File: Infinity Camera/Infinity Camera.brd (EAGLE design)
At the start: 115.6 x 54.6 mm, 7 parts

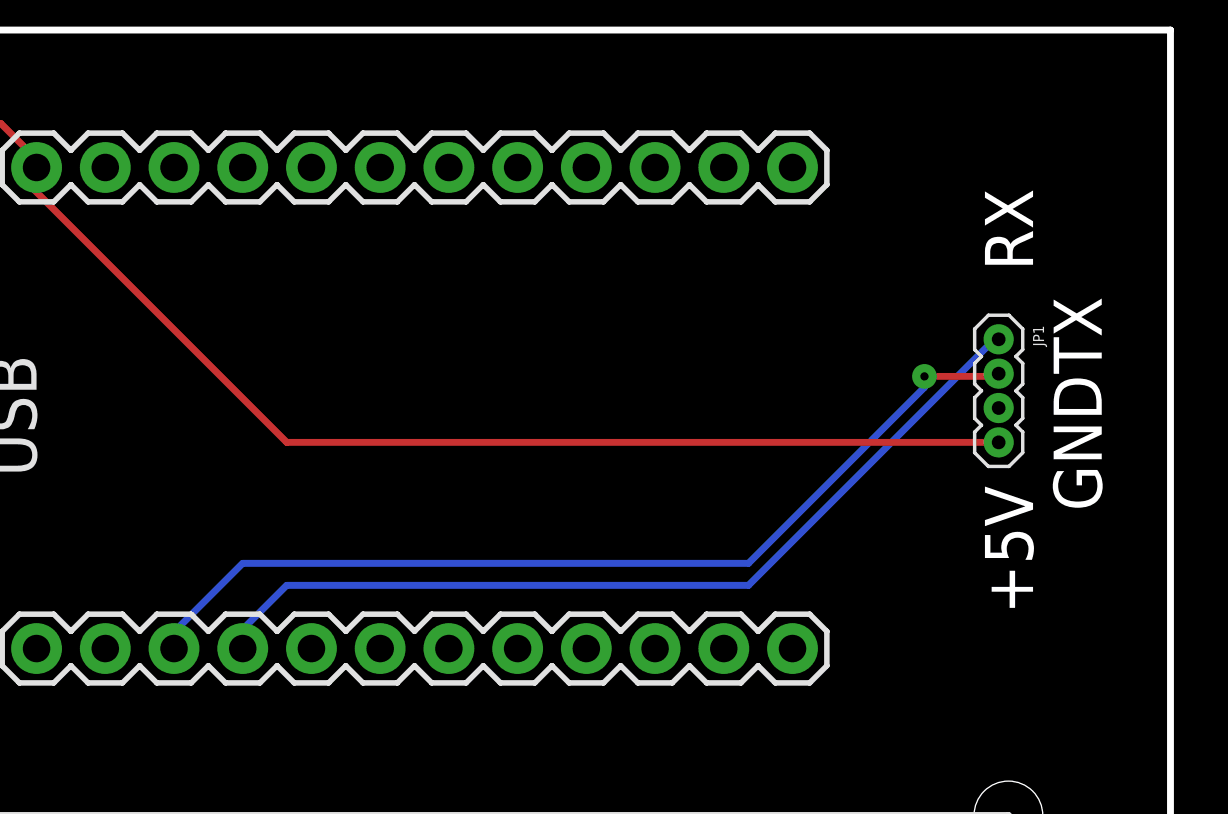
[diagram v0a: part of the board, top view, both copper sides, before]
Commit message: Reviewed Infinity Camera
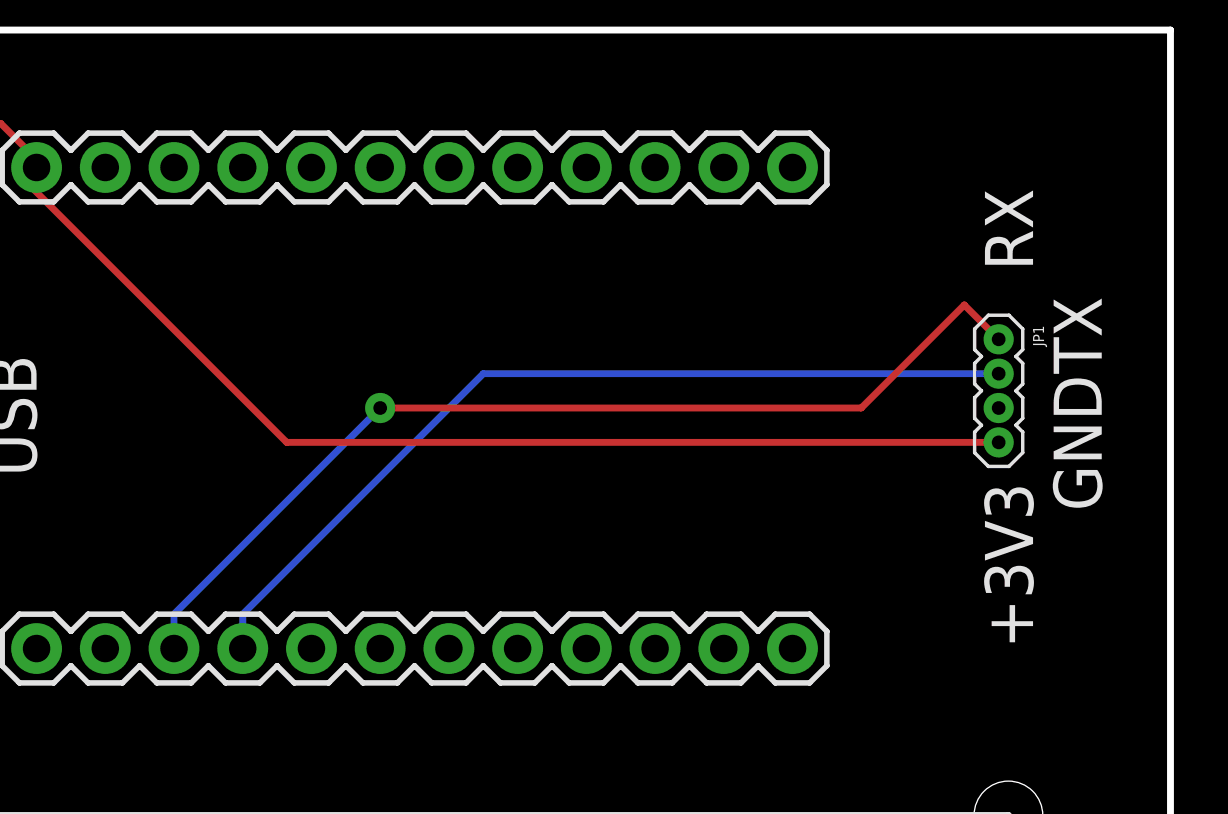
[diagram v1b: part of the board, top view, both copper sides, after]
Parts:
- added U$3: (no value), Spark:SPARK_LOGO
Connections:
- net +5V renamed +3V3
- removed net RX: JP1.1, U$1.4
- removed net TX: JP1.2, U$1.3
- new net CAMERA_RX: JP1.1, U$1.3
- new net CAMERA_TX: JP1.2, U$1.4
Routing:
- net CAMERA_RX: track 0.00 -> 37.0 mm, vias 0 -> 1
- net TX: track 35.5 -> 0.00 mm, vias 1 -> 0
- net RX: track 33.1 -> 0.00 mm
- net CAMERA_TX: track 0.00 -> 32.9 mm
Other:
- board text added: "+3V3"
- board text added: "Spark Infinity Camera v0.1 2013-04-08"
- board text removed: "+5V"
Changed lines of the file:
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@@
 <wire x1="125.73" y1="96.52" x2="125.73" y2="41.91" width="0.254" layer="20"/>
 <wire x1="125.73" y1="41.91" x2="10.16" y2="41.91" width="0.254" layer="20"/>
-<text x="120.65" y="74.93" size="1.778" layer="20" font="vector" ratio="15" rot="R90">+5V</text>
-<text x="123.19" y="78.74" size="1.778" layer="20" font="vector" ratio="15" rot="R90">GND</text>
-<text x="123.19" y="83.82" size="1.778" layer="20" font="vector" ratio="15" rot="R90">TX</text>
-<text x="120.65" y="87.63" size="1.778" layer="20" font="vector" ratio="15" rot="R90">RX</text>
+<text x="120.65" y="73.66" size="1.778" layer="21" font="vector" ratio="15" rot="R90">+3V3</text>
+<text x="123.19" y="78.74" size="1.778" layer="21" font="vector" ratio="15" rot="R90">GND</text>
+<text x="123.19" y="83.82" size="1.778" layer="21" font="vector" ratio="15" rot="R90">TX</text>
+<text x="120.65" y="87.63" size="1.778" layer="21" font="vector" ratio="15" rot="R90">RX</text>
 <wire x1="78.74" y1="46.99" x2="78.74" y2="67.49" width="0.254" layer="21"/>
 <wire x1="78.74" y1="67.49" x2="119.74" y2="67.49" width="0.254" layer="21"/>
@@
 <wire x1="119.74" y1="46.99" x2="78.74" y2="46.99" width="0.254" layer="21"/>
 <text x="83.82" y="80.01" size="1.778" layer="21" font="vector" ratio="15" rot="R90">USB</text>
+<text x="113.03" y="53.34" size="1.778" layer="22" font="vector" ratio="15" rot="MR0">Spark Infinity Camera
+v0.1
+2013-04-08</text>
 </plain>
 <attributes>
@@
 <element name="U$2" library="Spark" package="SPARK_LOGO" value="" x="7.62" y="5.08"/>
 <element name="JP1" library="SparkFun-Connectors" package="1X04-1.27MM" value="" x="119.38" y="85.09" rot="R270"/>
+<element name="U$3" library="Spark" package="SPARK_LOGO" value="" x="85.09" y="80.01"/>
 </elements>
 <signals>
-<signal name="+5V">
+<signal name="+3V3">
 <contactref element="POWER" pad="3"/>
 <contactref element="U$1" pad="24"/>
@@
 <contactref element="U$1" pad="1"/>
 </signal>
-<signal name="TX">
+<signal name="CAMERA_TX">
 <contactref element="JP1" pad="2"/>
+<contactref element="U$1" pad="4"/>
+<wire x1="91.44" y1="74.93" x2="91.44" y2="73.66" width="0.254" layer="16"/>
+<wire x1="100.33" y1="83.82" x2="91.44" y2="74.93" width="0.254" layer="16"/>
+<wire x1="119.38" y1="83.82" x2="100.33" y2="83.82" width="0.254" layer="16"/>
+</signal>
+<signal name="CAMERA_RX">
+<contactref element="JP1" pad="1"/>
 <contactref element="U$1" pad="3"/>
-<wire x1="116.6368" y1="83.7184" x2="119.0752" y2="83.7184" width="0.254" layer="1"/>
-<wire x1="116.6368" y1="83.312" x2="116.6368" y2="83.7184" width="0.254" layer="16"/>
-<wire x1="110.1344" y1="76.8096" x2="116.6368" y2="83.312" width="0.254" layer="16"/>
-<wire x1="91.44" y1="76.8096" x2="110.1344" y2="76.8096" width="0.254" layer="16"/>
-<wire x1="88.5952" y1="73.9648" x2="91.44" y2="76.8096" width="0.254" layer="16"/>
-<wire x1="119.0752" y1="83.7184" x2="119.38" y2="83.82" width="0.254" layer="1"/>
-<wire x1="88.5952" y1="73.9648" x2="88.9" y2="73.66" width="0.254" layer="16"/>
-<via x="116.6368" y="83.7184" extent="1-16" drill="0.3048"/>
-</signal>
-<signal name="RX">
-<contactref element="JP1" pad="1"/>
-<contactref element="U$1" pad="4"/>
-<wire x1="110.1344" y1="75.9968" x2="119.0752" y2="84.9376" width="0.254" layer="16"/>
-<wire x1="93.0656" y1="75.9968" x2="110.1344" y2="75.9968" width="0.254" layer="16"/>
-<wire x1="91.44" y1="74.3712" x2="93.0656" y2="75.9968" width="0.254" layer="16"/>
-<wire x1="91.44" y1="73.66" x2="91.44" y2="74.3712" width="0.254" layer="16"/>
-<wire x1="119.0752" y1="84.9376" x2="119.38" y2="85.09" width="0.254" layer="16"/>
+<wire x1="88.9" y1="74.93" x2="88.9" y2="73.66" width="0.254" layer="16"/>
+<wire x1="96.52" y1="82.55" x2="88.9" y2="74.93" width="0.254" layer="16"/>
+<wire x1="114.3" y1="82.55" x2="96.52" y2="82.55" width="0.254" layer="1"/>
+<wire x1="118.11" y1="86.36" x2="114.3" y2="82.55" width="0.254" layer="1"/>
+<wire x1="119.38" y1="85.09" x2="118.11" y2="86.36" width="0.254" layer="1"/>
+<via x="96.52" y="82.55" extent="1-16" drill="0.508"/>
 </signal>
 </signals>
 </board>
 </drawing>
+<compatibility>
+<note version="6.3" minversion="6.2.2" severity="warning">
+Since Version 6.2.2 text objects can contain more than one line,
+which will not be processed correctly with this version.
+</note>
+</compatibility>
 </eagle>

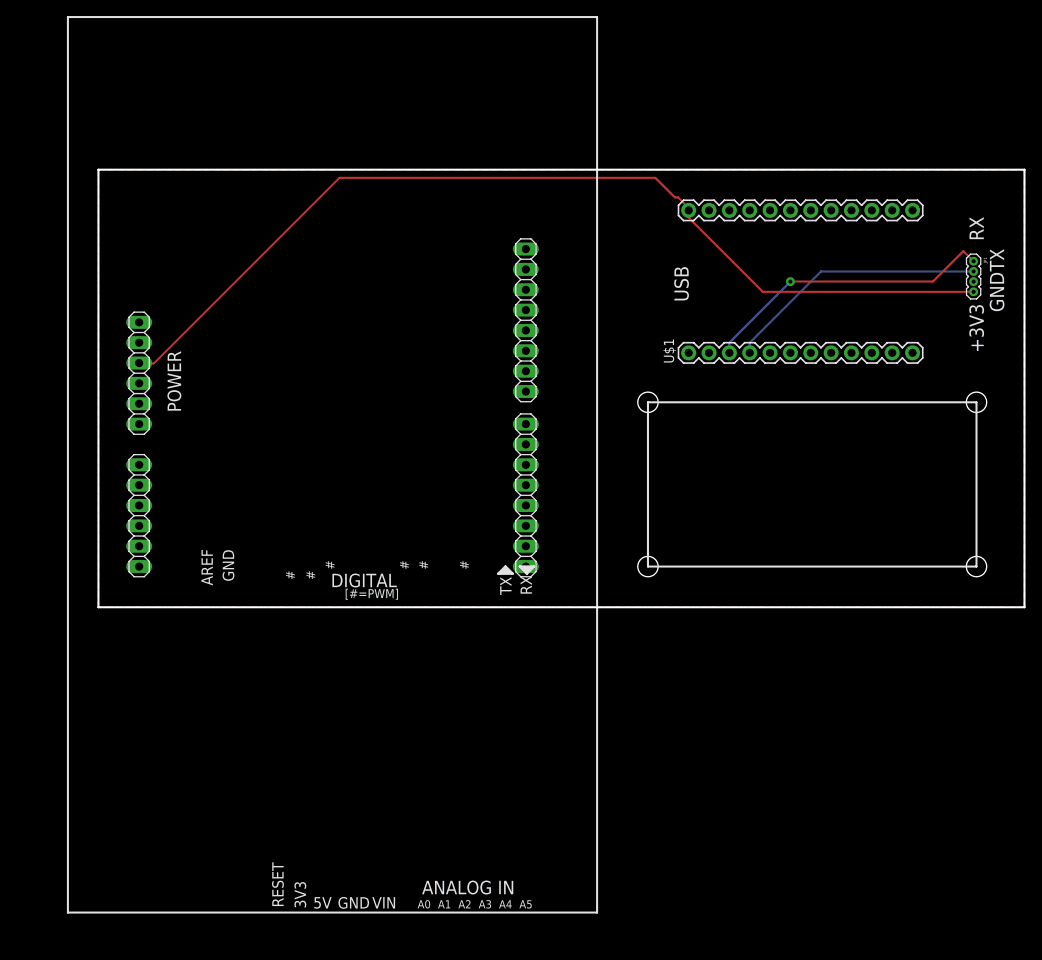
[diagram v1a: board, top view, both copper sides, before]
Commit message: Started adding transistor to the Inifinity Camera.  Still needs to be finished.  Generated Gerber files for the LCD Shield and had it spun up.  Infinity camera gerber files need to be updated upon completion
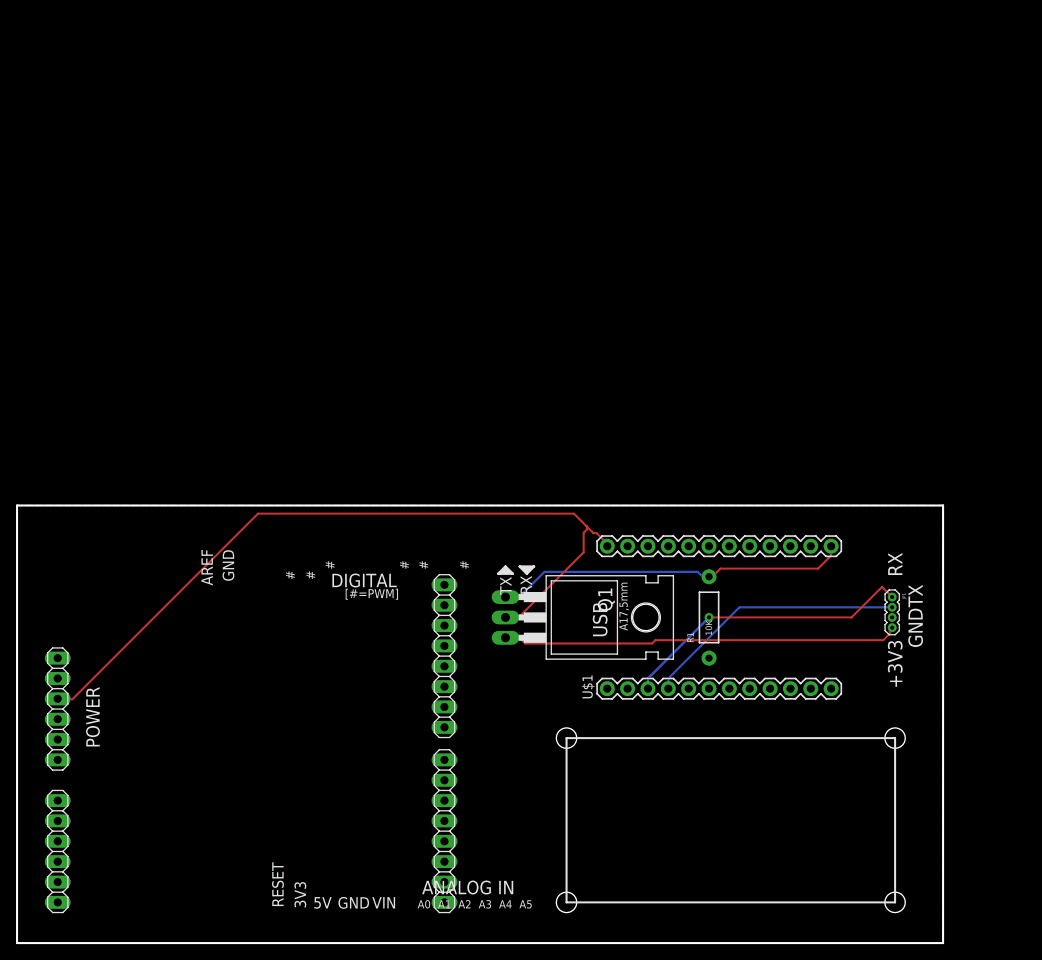
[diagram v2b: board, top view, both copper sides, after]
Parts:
- added Q1: IRLZ44Z, transistor-power:TO220BH
- added R1: 10K, SparkFun-Resistors:AXIAL-0.4
- moved AD 43.1 mm to (5.08, 11.4)
- moved POWER 43.1 mm to (5.08, 29.2)
- moved IOH 43.1 mm to (53.3, 35.8)
- moved IOL 43.1 mm to (53.3, 14.0)
- moved JP1 43.1 mm to (109.2, 43.2)
- moved U$1 43.1 mm to (87.6, 40.6)
- moved U$3 43.1 mm to (74.9, 38.1)
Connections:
- new net CAMERA_3V3: JP1.4, Q1.S
- new net N$1: Q1.G, R1.P$2, U$1.13
- net +3V3: now also Q1.D; no longer JP1.4
- net GND: now also R1.P$1
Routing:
- net CAMERA_3V3: track 0.00 -> 49.8 mm
- net N$1: track 0.00 -> 44.8 mm
- net +3V3: track 120.9 -> 97.1 mm

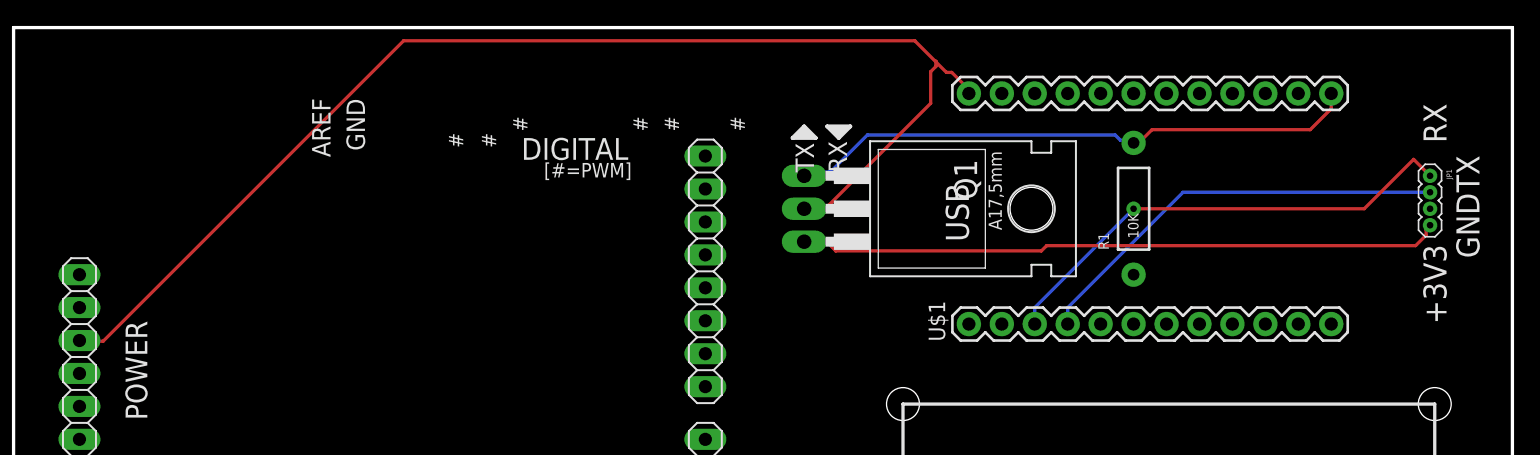
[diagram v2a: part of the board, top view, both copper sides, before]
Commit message: Updated infinity camera with transistor and recreated Gerber files
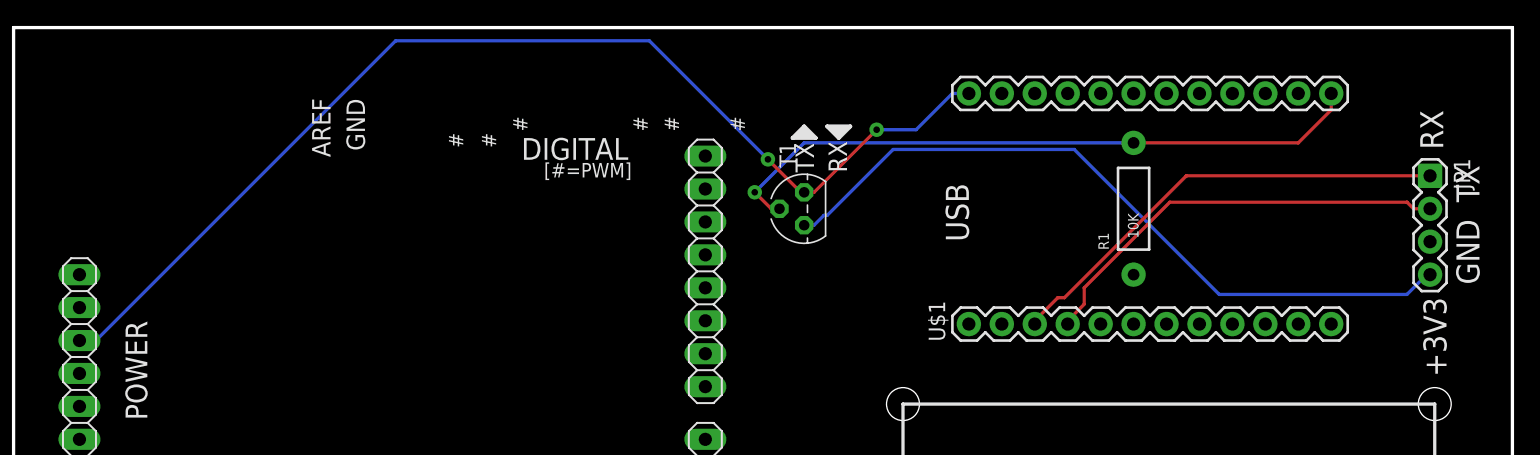
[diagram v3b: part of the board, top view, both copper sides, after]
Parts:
- removed Q1: IRLZ44Z, transistor-power:TO220BH
- added T1: 2N3904, transistor:TO92
- JP1: device SparkFun-Connectors:1X04-1.27MM -> SparkFun-Connectors:1X04
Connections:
- net +3V3: now also T1.1; no longer Q1.D
- net CAMERA_3V3: now also T1.3; no longer Q1.S
- net N$1: now also T1.2; no longer Q1.G
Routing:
- net +3V3: track 97.1 -> 86.2 mm, vias 0 -> 2
- net CAMERA_3V3: track 49.8 -> 55.9 mm
- net N$1: track 44.8 -> 50.8 mm, vias 0 -> 1
- net CAMERA_RX: track 37.0 -> 35.4 mm, vias 1 -> 0
